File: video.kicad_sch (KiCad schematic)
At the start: 16 parts, among them IC1 MC3346, IC2 MC3346, IC3 MC3346

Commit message: video tracing
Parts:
- added R10, R12, R14, R8: 220R, Dragon:R_Axial_DIN0309_L9.0mm_D2.5mm_P12.70mm_Horizontal, symbol Device:R_Small
- added R40: 500R, Dragon:R_Axial_DIN0309_L9.0mm_D2.5mm_P12.70mm_Horizontal, symbol Device:R_Small
- added R47, R48: 2R2, Dragon:R_Axial_DIN0309_L9.0mm_D2.5mm_P12.70mm_Horizontal, symbol Device:R_Small
- added T1, T2, T3, T4: Q_NPN_CBE, Package_TO_SOT_THT:TO-92, symbol Device:Q_NPN_CBE
- added UM1: ~, Dragon:RF_Modulator_Astec_UM1601, symbol vdg:RF_Modulator
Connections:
- net at R39.2: now also UM1.1 (Bias)
- net ic3_4: now reaches C17.1
- net ic3_4: now also C19.1, IC3.4
- net ic3_11: now reaches C14.1
- net ic3_11: now also C15.2, IC3.11, L1.3
- net ic3_8: now reaches C14.2
- net ic3_8: now also IC3.8, L1.1, R40.2, R47.2
- net GND: now reaches L1.5 (GND)
- net GND: now also UM1.4 (GND)
- net at C19.2: now also R48.1
- net at C13.1, R36.1: now also UM1.3 (Audio)
- net at IC3.14: now also IC3.3
- net at IC3.2: now also IC3.9
- net ic3_5: now reaches IC3.5
- net ic3_5: now also R47.1, UM1.2 (Composite)
- new net pl11_4: R8.1
- new net pl11_5: R10.1
- new net pl11_6: R14.1
- new net pl11_7: R12.1
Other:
- moved on the sheet: C13, C14, C15, C19, R36, R39

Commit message: more video tracing
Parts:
- added C2: 100nF, Capacitor_THT:C_Disc_D4.3mm_W1.9mm_P5.00mm, symbol Device:C_Small
- added D9: 1N, Diode_THT:D_A-405_P12.70mm_Horizontal, symbol Device:D
- added R11, R13, R15, R16, R17, R19, R21, R22, R23, R24, R25, R26, R27, R28, R29, R30, R31, R32, R33, R34, R35, R37, R38, R41, R42, R43, R44, R45, R46, R49, R50, R6, R7, R9: 220R, Dragon:R_Axial_DIN0309_L9.0mm_D2.5mm_P12.70mm_Horizontal, symbol Device:R_Small
- added R18, R20: 220R, Resistor_THT:R_Axial_DIN0207_L6.3mm_D2.5mm_P10.16mm_Horizontal, symbol Device:R_Small
- C11: footprint Capacitor_THT:C_Disc_D4.3mm_W1.9mm_P5.00mm -> Capacitor_THT:C_Disc_D3.0mm_W2.0mm_P2.50mm
- T1, T2, T3, T4: footprint Package_TO_SOT_THT:TO-92 -> Package_TO_SOT_THT:TO-92_Wide
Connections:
- net GND: now also C10.2, C18.1, R43.1, R44.1, R46.1, R50.2
- net ic3_4: now also R45.1
- net ic3_8: now also IC3.1
- net at R14.2: now also T4.3 (E), R25.1
- net ic1_1: now reaches IC1.1
- net ic1_1: now also R6.2
- net ic1_10: now reaches IC1.10
- net ic1_10: now also R29.2, R31.2
- net ic1_12: now reaches IC1.12
- net ic1_12: now also R31.1, R32.1, R34.2, R35.1
- net ic1_13: now reaches IC1.13
- net ic1_13: now also R33.1
- net ic1_14: now reaches IC1.14
- net ic1_14: now also IC2.3, R15.1, R16.1
- net ic1_7: now reaches IC1.7
- net ic1_7: now also R30.1, R32.2
- net +5V: now reaches IC1.8
- net +5V: now also IC2.14, R36.2, T1.1 (C), T2.1 (C), T3.1 (C), T4.1 (C), R11.2, R13.2, R15.2, R37.2, R6.1, R7.2, R9.2
- net ic3_2: now reaches C17.2
- net ic3_2: now also IC3.2, IC3.9, R40.1, R45.2
- net ic2_11: now reaches T2.2 (B)
- net ic2_11: now also IC2.11, R7.1
- net at T2.3 (E): now also R10.2, R27.1
- net at C16.1: now also IC3.6
- net at C16.2: now also IC3.12, R42.2, R43.2
- net at R12.2: now also T1.3 (E), R28.1
- net at R8.2: now also T3.3 (E), R23.1
- net ic2_8: now reaches T4.2 (B)
- net ic2_8: now also IC2.8, R11.1
- net ic2_1: now reaches IC2.1
- net ic2_1: now also T3.2 (B), R9.1
- net ic2_10: now reaches IC2.10
- net ic2_10: now also R26.2, R30.2
- net ic2_12: now reaches IC2.12
- net ic2_13: now reaches IC2.13
- net ic2_13: now also R16.2, R22.1, R24.2, R26.1
- net ic2_6: now reaches IC2.2
- net ic2_6: now also IC2.4, IC2.6, IC2.9, R35.2
- net ic2_5: now reaches IC2.5
- net ic2_5: now also T1.2 (B), R13.1
- net ic2_7: now reaches IC2.7
- net ic2_7: now also R24.1, R29.1
- net at C15.1: now also R41.2
- net at C18.2: now also R41.1, R42.1
- net SOUND: now reaches R48.2
- net SOUND: now also R49.2
- net at IC3.10: now also IC3.7, R44.2
- net at IC3.13: now also R46.2
- new net +12V: R38.2
- new net -5V: R18.2, R20.2, R22.2, R23.2, R25.2, R27.2, R28.2, R33.2, R34.1
- new net pl11_1: R38.1
- new net pl11_2: R37.1
- new net pl11_3: R49.1, R50.1
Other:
- moved on the sheet: C10, C13, C15, C16, C17, C18, IC1, IC2, R10, R12, R14, R36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

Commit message: power tracing
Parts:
- removed C2: 100nF, Capacitor_THT:C_Disc_D4.3mm_W1.9mm_P5.00mm, symbol Device:C_Small
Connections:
- net ic2_6 is gone; now on net GND: IC2.2, IC2.4, IC2.6, IC2.9, R35.2
- net +5V: now also IC1.11
- net GND: now also R17.1, R19.1, R21.1
- net LUMA: now also C10.1
- net ic1_1: now also C12.1
- net ic2_12: now also C12.2, D9.1 (K)
- net at R21.2: now also D9.2 (A), R20.1
- net ic1_3: now reaches IC1.3
- net ic1_3: now also C11.2, R18.1, R19.2
- net at C11.1: now also R17.2
- no-connect marks 0 -> 2
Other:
- moved on the sheet: C11, C12, D9, R17, R18, R19, R20, R21

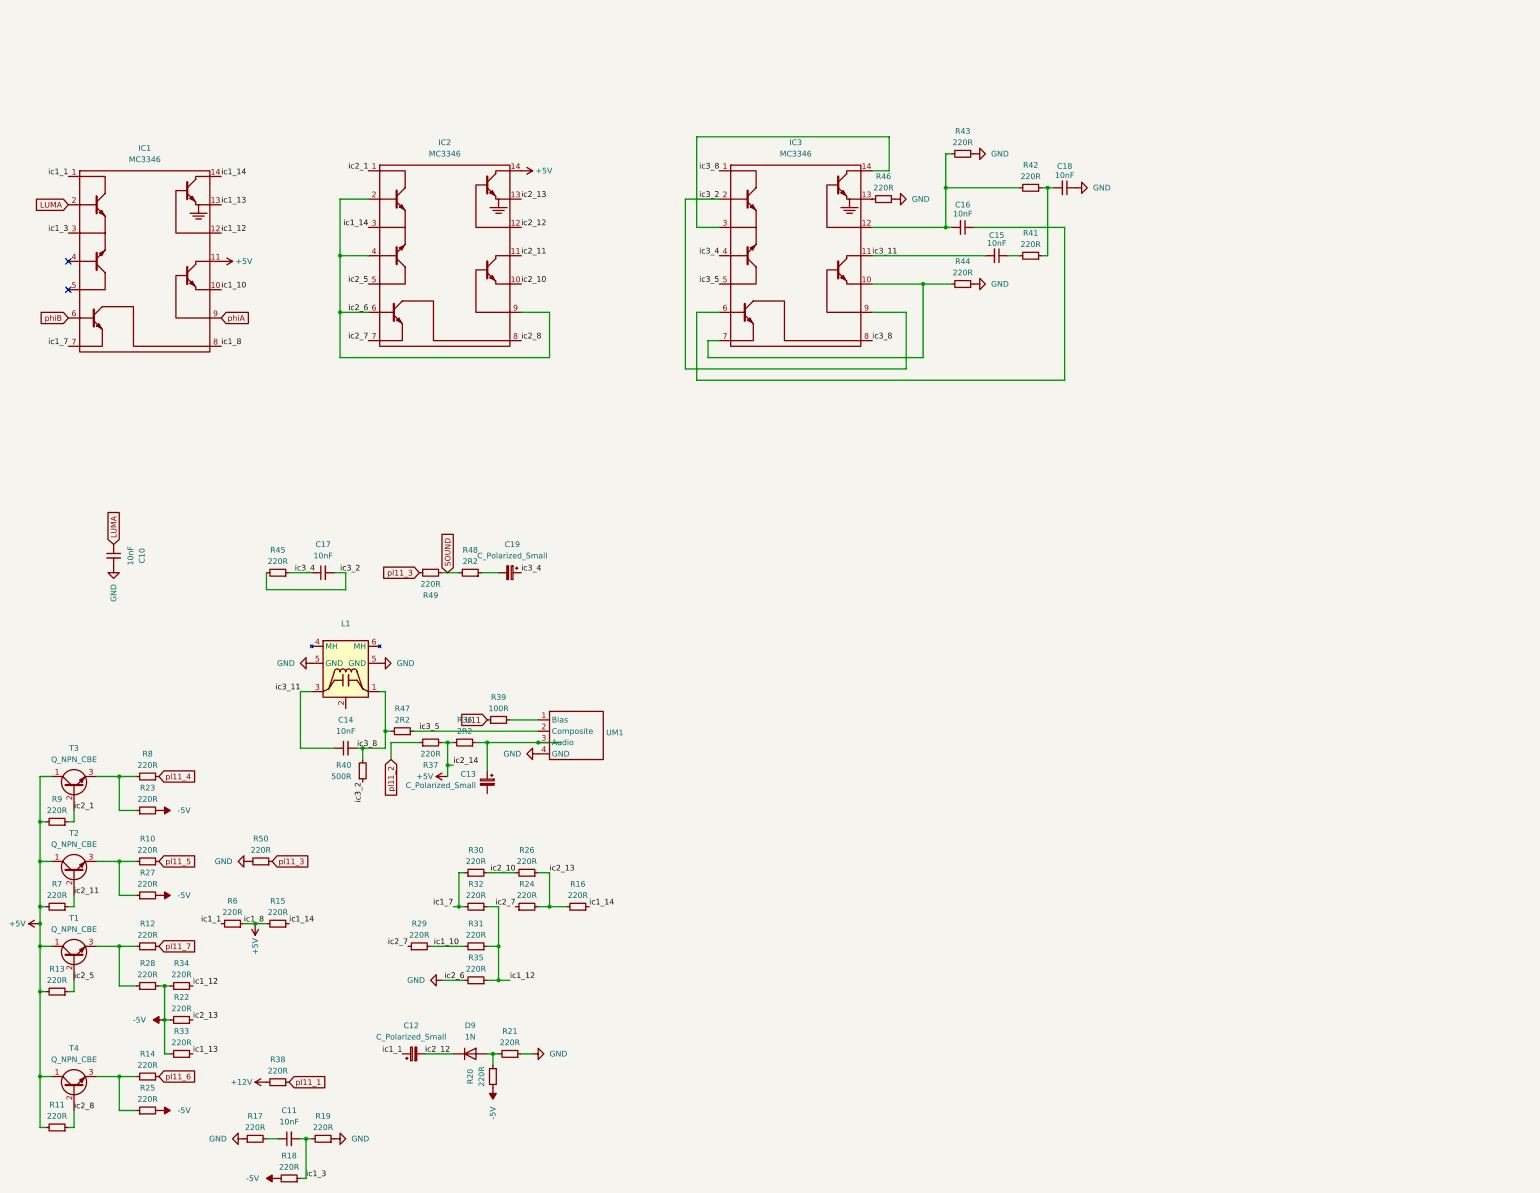
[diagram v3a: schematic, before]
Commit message: layout and routing complete
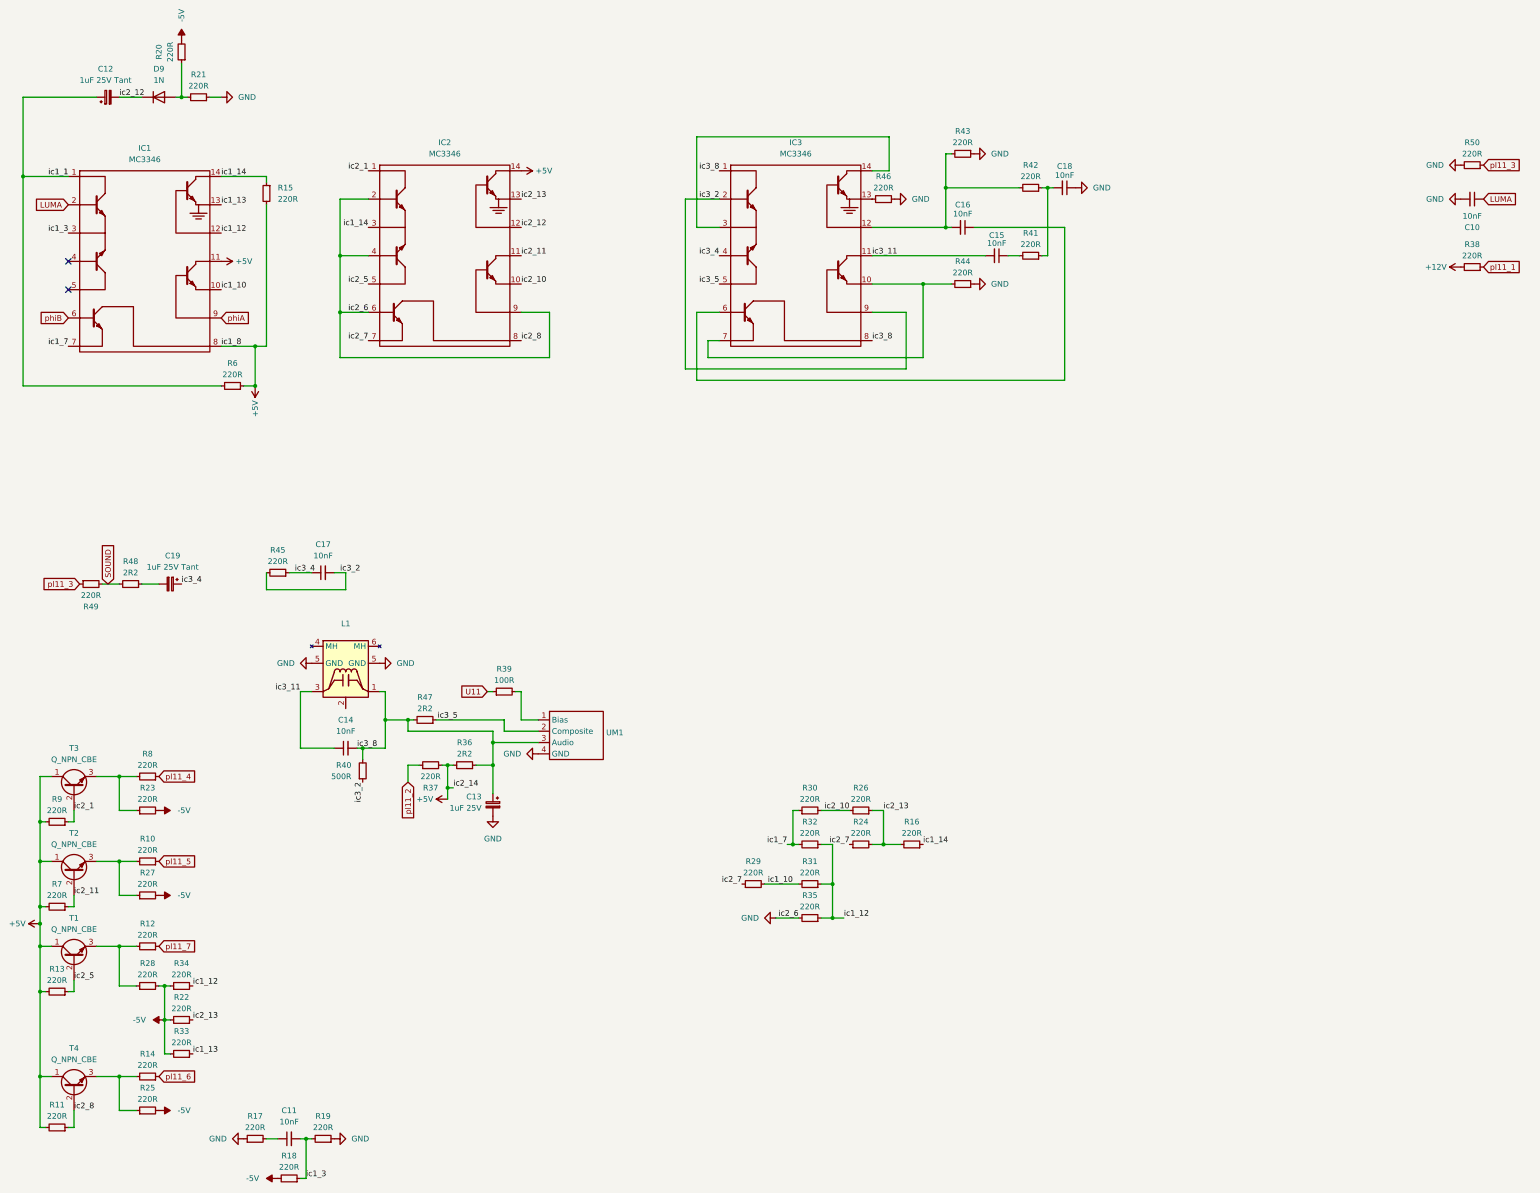
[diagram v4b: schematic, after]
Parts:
- C12, C19: value C_Polarized_Small -> 1uF 25V Tant
- C13: value C_Polarized_Small -> 1uF 25V
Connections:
- net GND: now also C13.2
- net ic3_8: now also C13.1, R36.1, UM1.3 (Audio)
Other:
- moved on the sheet: C10, C12, C13, C19, D9, R15, R16, R20, R21, R24, R26, R29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
